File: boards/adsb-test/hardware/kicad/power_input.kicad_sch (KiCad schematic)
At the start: 19 parts, among them J201 User USB-C (PD sink), Q201 FDS9435A, U201 STUSB4500QTR, U202 USBLC6-2SC6

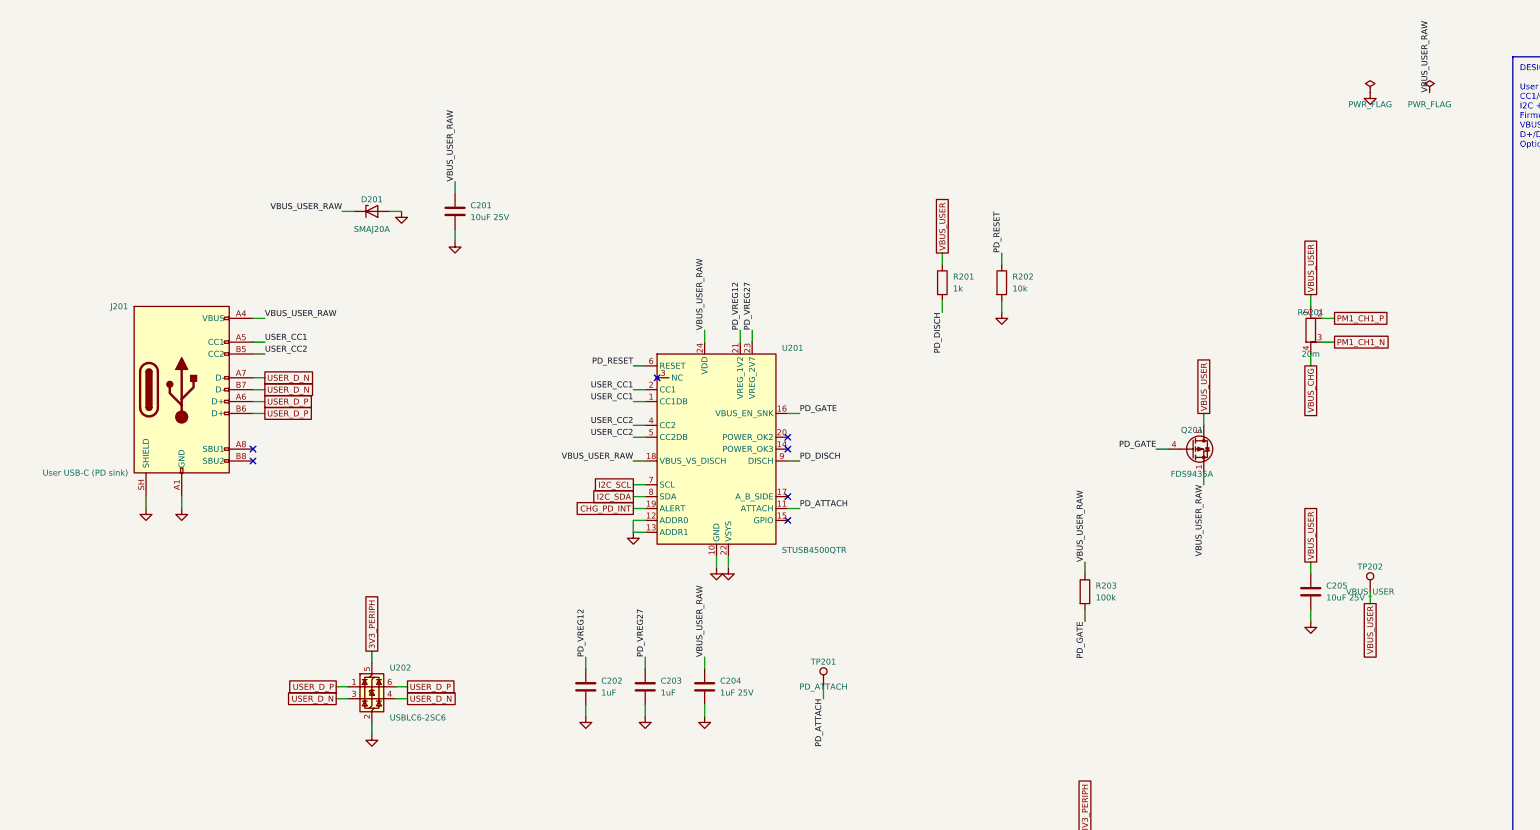
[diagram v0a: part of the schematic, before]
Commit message: ADSB_Test: User USB-C on its own sheet, RP2040 GPIO header + optional I2C, shunt/PWR_FLAG text fixed
Co-Authored-By: Claude Opus 5.5 <noreply@anthropic.com>
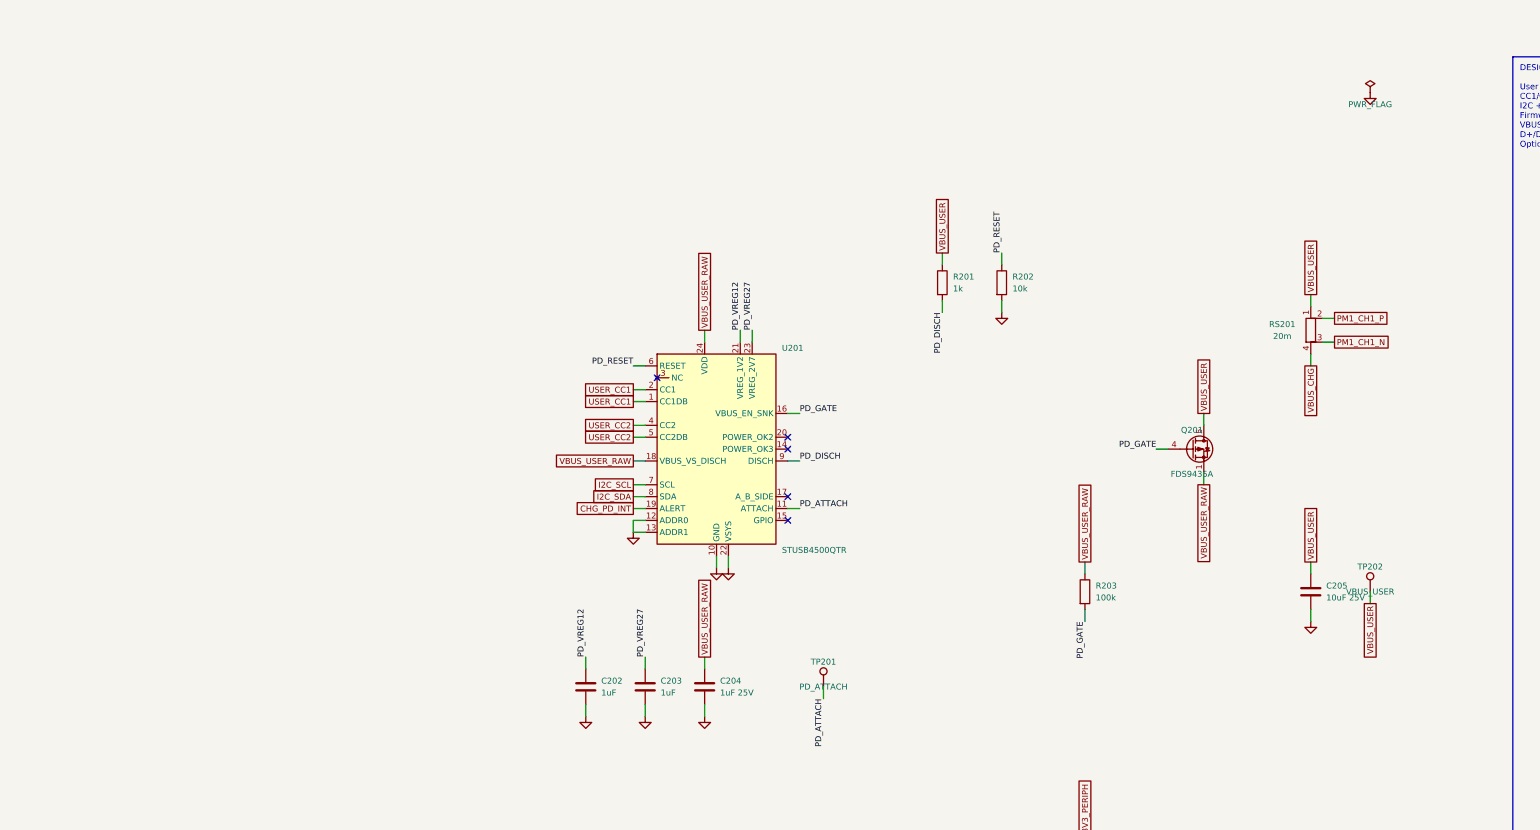
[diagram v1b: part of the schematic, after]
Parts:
- removed C201: 10uF 25V, Capacitor_SMD:C_0805_2012Metric_Pad1.18x1.45mm_HandSolder, symbol Device:C
- removed D201: SMAJ20A, Diode_SMD:D_SMA, symbol Device:D_Zener
- removed J201: User USB-C (PD sink), Connector_USB:USB_C_Receptacle_GCT_USB4105-xx-A_16P_TopMnt_Horizontal, symbol Connector:USB_C_Receptacle_USB2.0_16P
- removed U202: USBLC6-2SC6, Package_TO_SOT_SMD:SOT-23-6_Handsoldering, symbol Power_Protection:USBLC6-2SC6
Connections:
- no-connect marks 7 -> 5

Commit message: ADSB_Test: Dev port split over three A3 sheets; old note boxes replaced with short current notes
Co-Authored-By: Claude Opus 5.5 <noreply@anthropic.com>
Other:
- note added: "POWER INPUT: User USB-C (on the User USB-C sheet) -> STUSB4500 PD sink (NVM: 5 V / 9 V / 15 V at 3 A, I2C 0x28). VBUS_EN_SNK drives the FDS9435A P-FET (SO-8), so VBUS_USER only appears once a contract is in place. RS201 (20 mR) -> PM1 CH1. JP201 (default open) lets the Dev USB VBUS feed the charger for bench work. VSYS (pin 22) is tied to GND as DS12499 says when unused; ALERT is wired-OR with th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"

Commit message: ADSB_Test: Kelvin shunt footprint, Wi-Fi RP-SMA on the top edge, PCB parity 0
- Shunts RS201-RS409: 4-pad R_Shunt_1206_Kelvin_HandSolder (net-tied sense
  pads) replaces the 2-pad 1206, which put the sense net on the load pad.
- Wi-Fi: module IPEX -> U.FL jumper -> J601 -> J602 RP-SMA on the top long
  edge, away from the 1090/978 and GNSS SMAs. BOM, datasheets, docs.
- gen_pcb: symbol fields and BOM flags copied to footprints, unconnected
  net names escaped; top-edge placement.

Co-Authored-By: Claude Opus 5.5 <noreply@anthropic.com>
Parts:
- RS201: footprint Resistor_SMD:R_1206_3216Metric_Pad1.30x1.75mm_HandSolder -> ADSB_Test:R_Shunt_1206_Kelvin_HandSolder; Check Kelvin-route pins 2/3 to the PAC1954 -> Route sense pads 2/3 to the PAC1954 as a pair
